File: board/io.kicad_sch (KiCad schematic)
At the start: 14 parts, among them J4 DE9_Socket, J5 DE9_Socket, U15 68681, U16 MAX232, Y2 3.6864MHz

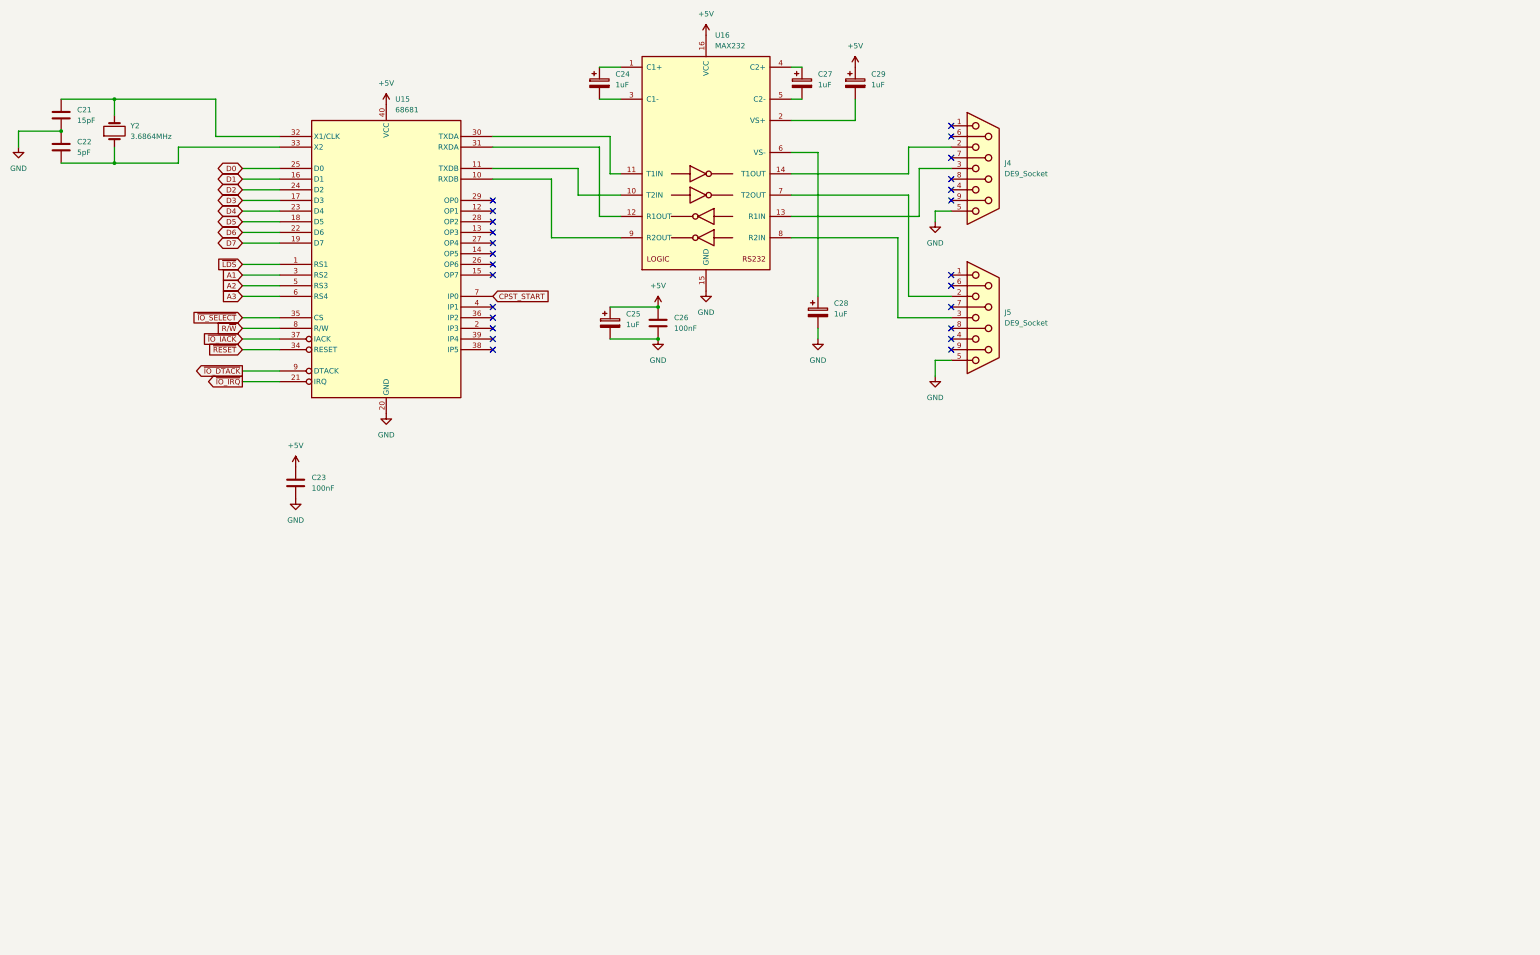
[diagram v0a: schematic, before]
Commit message: change IO to 8051 variant, add audio
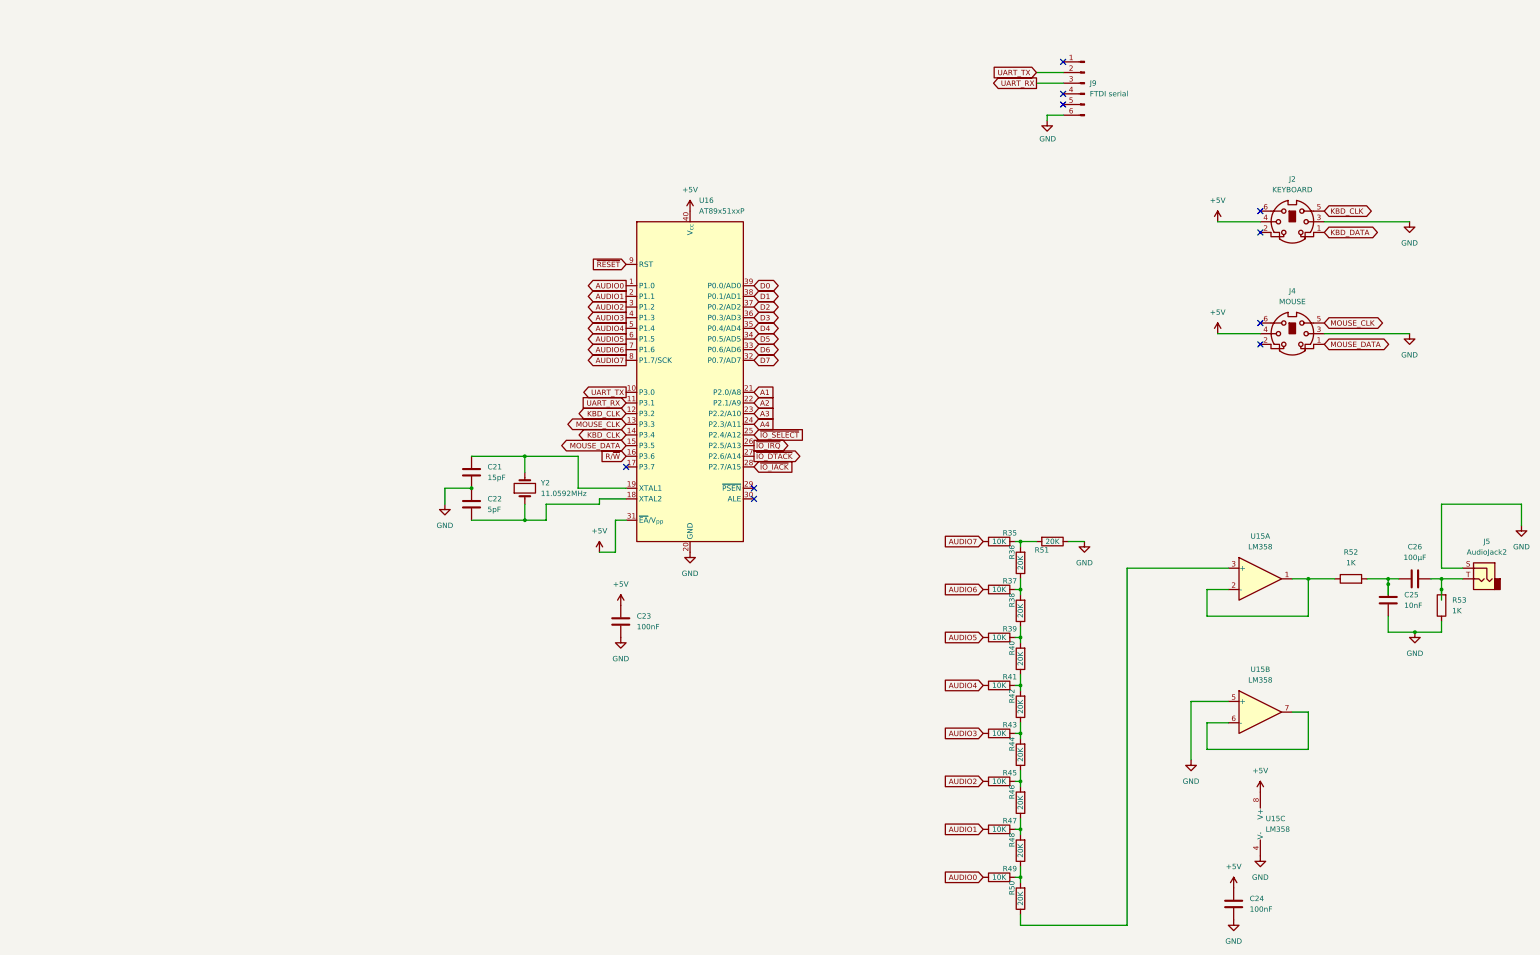
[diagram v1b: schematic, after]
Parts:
- removed C24, C25, C27, C28, C29: 1uF, symbol Device:C_Polarized
- removed J4, J5: DE9_Socket, symbol Connector:DE9_Socket
- removed U15: 68681, symbol Interface:68681
- removed U16: MAX232, symbol Interface_UART:MAX232
- added C24: 100nF, symbol Device:C
- added C25: 10nF, symbol Device:C
- added J2: KEYBOARD, symbol Connector:Mini-DIN-6
- added J4: MOUSE, symbol Connector:Mini-DIN-6
- added J5: AudioJack2, symbol Connector_Audio:AudioJack2
- added J9: FTDI serial, symbol Connector:Conn_01x06_Pin
- added R35, R37, R39, R41, R43, R45, R47, R49: 10K, symbol Device:R
- added R36, R38, R40, R42, R44, R46, R48, R50, R51: 20K, symbol Device:R
- added R52, R53: 1K, symbol Device:R
- added U15: LM358, symbol Amplifier_Operational:LM358
- added U16: AT89x51xxP, Package_DIP:DIP-40_W15.24mm, symbol MCU_Microchip_8051:AT89x51xxP
- C26: value 100nF -> 100µF
- Y2: value 3.6864MHz -> 11.0592MHz
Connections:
- net +5V: now also C24.1, J2.4, J4.4, U15.8 (V+), U16.31 (~{EA}/V_{pp}), U16.40 (V_{cc}); no longer C26.1
- net A1: now also U16.21 (P2.0/A8)
- net A2: now also U16.22 (P2.1/A9)
- net A3: now also U16.23 (P2.2/A10)
- net D0: now also U16.39 (P0.0/AD0)
- net D1: now also U16.38 (P0.1/AD1)
- net D2: now also U16.37 (P0.2/AD2)
- net D3: now also U16.36 (P0.3/AD3)
- net D4: now also U16.35 (P0.4/AD4)
- net D5: now also U16.34 (P0.5/AD5)
- net D6: now also U16.33 (P0.6/AD6)
- net D7: now also U16.32 (P0.7/AD7)
- net GND: now also C24.2, C25.2, J2.3, J4.3, J5.S, J9.6 (Pin_6), R51.1, R53.1, U15.4 (V-), U15.5 (+), U16.20 (GND); no longer C26.2
- net R/~{W}: now also U16.16 (P3.6)
- net ~{IO_DTACK}: now also U16.27 (P2.6/A14)
- net ~{IO_IACK}: now also U16.28 (P2.7/A15)
- net ~{IO_IRQ}: now also U16.26 (P2.5/A13)
- net ~{IO_SELECT}: now also U16.25 (P2.4/A12)
- net ~{RESET}: now also U16.9 (RST)
- net at C21.1, Y2.2: now also U16.19 (XTAL1)
- net at C22.2, Y2.1: now also U16.18 (XTAL2)
- new net: R35.2, R36.2, R51.2
- new net: C25.1, C26.1, R52.2
- new net: C26.2, J5.T, R53.2
- new net: R36.1, R37.2, R38.2
- new net: R44.1, R45.2, R46.2
- new net: R42.1, R43.2, R44.2
- new net: R40.1, R41.2, R42.2
- new net: R38.1, R39.2, R40.2
- new net: U15.6 (-), U15.7
- new net: R46.1, R47.2, R48.2
- new net: R48.1, R49.2, R50.2
- new net: R52.1, U15.1, U15.2 (-)
- new net: R50.1, U15.3 (+)
- new net A4: U16.24 (P2.3/A11)
- new net AUDIO0: R49.1, U16.1 (P1.0)
- new net AUDIO1: R47.1, U16.2 (P1.1)
- new net AUDIO2: R45.1, U16.3 (P1.2)
- new net AUDIO3: R43.1, U16.4 (P1.3)
- new net AUDIO4: R41.1, U16.5 (P1.4)
- new net AUDIO5: R39.1, U16.6 (P1.5)
- new net AUDIO6: R37.1, U16.7 (P1.6)
- new net AUDIO7: R35.1, U16.8 (P1.7/SCK)
- new net KBD_CLK: J2.5, U16.12 (P3.2), U16.14 (P3.4)
- new net KBD_DATA: J2.1
- new net MOUSE_CLK: J4.5, U16.13 (P3.3)
- new net MOUSE_DATA: J4.1, U16.15 (P3.5)
- new net UART_RX: J9.3 (Pin_3), U16.11 (P3.1)
- new net UART_TX: J9.2 (Pin_2), U16.10 (P3.0)
- no-connect marks 25 -> 10
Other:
- moved on the sheet: C21, C22, C23, Y2

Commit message: design draft complete, added footprints
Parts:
- removed J5: AudioJack2, symbol Connector_Audio:AudioJack2
- added J5: AudioJack3, Connector_Audio:Jack_3.5mm_CUI_SJ1-3523N_Horizontal, symbol Connector_Audio:AudioJack3
- added R57, R58: 100, Resistor_THT:R_Axial_DIN0207_L6.3mm_D2.5mm_P10.16mm_Horizontal, symbol Device:R
- C21, C25: footprint (none) -> Capacitor_THT:C_Disc_D3.0mm_W1.6mm_P2.50mm
- C22: value 5pF -> 15pF; footprint (none) -> Capacitor_THT:C_Disc_D3.0mm_W1.6mm_P2.50mm
- C23, C24: footprint (none) -> Capacitor_THT:C_Disc_D5.0mm_W2.5mm_P5.00mm
- C26: footprint (none) -> Capacitor_THT:CP_Radial_D5.0mm_P2.50mm
- J2, J4: footprint (none) -> board:Mini_din6
- J9: footprint (none) -> Connector_PinHeader_2.54mm:PinHeader_1x06_P2.54mm_Vertical
- R35, R36, R37, R38, R39, R40, R41, R42, R43, R44, R45, R46, R47, R48, R49, R50, R51, R52, R53: footprint (none) -> Resistor_THT:R_Axial_DIN0207_L6.3mm_D2.5mm_P10.16mm_Horizontal
- U15: footprint (none) -> Package_DIP:DIP-8_W7.62mm
- Y2: footprint (none) -> Crystal:Resonator-2Pin_W10.0mm_H5.0mm
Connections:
- net GND: now also J5.S
- net KBD_CLK: no longer U16.14 (P3.4)
- net KBD_DATA: now also U16.14 (P3.4)
- net at C26.2, R53.2: now also R57.2, R58.2
- new net: J5.R, R57.1
- new net: J5.T, R58.1

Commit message: start of PCB and MMU
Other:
- moved on the sheet: C21, C22, C23, C24, C25, C26, J2, J4, J5, J9, R35, R36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

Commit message: checkpoint
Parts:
- removed R35, R37, R39, R41, R43, R45, R47, R49: 10K, Resistor_THT:R_Axial_DIN0207_L6.3mm_D2.5mm_P10.16mm_Horizontal, symbol Device:R
- removed R36, R38, R40, R42, R44, R46, R48, R50, R51: 20K, Resistor_THT:R_Axial_DIN0207_L6.3mm_D2.5mm_P10.16mm_Horizontal, symbol Device:R
- added R60: 4610X-R2R-103LF, board:BO_4610X, symbol 68k_board:4610X-R2R-103LF
- J2, J4: symbol Connector:Mini-DIN-6 -> 68k_board:Mini-DIN-6-GroundPins
- J9: footprint Connector_PinHeader_2.54mm:PinHeader_1x06_P2.54mm_Vertical -> Connector_PinHeader_2.54mm:PinHeader_1x06_P2.54mm_Horizontal
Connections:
- net AUDIO0: now also R60.9
- net AUDIO1: now also R60.8
- net AUDIO2: now also R60.7
- net AUDIO3: now also R60.6
- net AUDIO4: now also R60.5
- net AUDIO5: now also R60.4
- net AUDIO6: now also R60.3
- net AUDIO7: now also R60.2
- net GND: now also J2.7 (GND), J4.7 (GND), R60.10
- net at U15.3 (+): now also R60.1

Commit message: checkpoint
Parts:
- removed C24: 100nF, Capacitor_THT:C_Disc_D5.0mm_W2.5mm_P5.00mm, symbol Device:C
- removed C25: 10nF, Capacitor_THT:C_Disc_D3.0mm_W1.6mm_P2.50mm, symbol Device:C
- removed C26: 100µF, Capacitor_THT:CP_Radial_D5.0mm_P2.50mm, symbol Device:C
- removed J5: AudioJack3, Connector_Audio:Jack_3.5mm_CUI_SJ1-3523N_Horizontal, symbol Connector_Audio:AudioJack3
- removed R52, R53: 1K, Resistor_THT:R_Axial_DIN0207_L6.3mm_D2.5mm_P10.16mm_Horizontal, symbol Device:R
- removed R57, R58: 100, Resistor_THT:R_Axial_DIN0207_L6.3mm_D2.5mm_P10.16mm_Horizontal, symbol Device:R
- removed R60: 4610X-R2R-103LF, board:BO_4610X, symbol 68k_board:4610X-R2R-103LF
- removed U15: LM358, Package_DIP:DIP-8_W7.62mm, symbol Amplifier_Operational:LM358
- added R7, R9: 10K, Resistor_THT:R_Axial_DIN0207_L6.3mm_D2.5mm_P10.16mm_Horizontal, symbol Device:R
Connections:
- net ~{IO_SELECT} is gone; now on net ~{IO_IRQ}: U16.25 (P2.4/A12)
- net +5V: now also R7.1, R9.1
- net KBD_CLK: now also U16.13 (P3.3); no longer U16.12 (P3.2)
- net KBD_DATA: now also U16.12 (P3.2); no longer U16.14 (P3.4)
- net MOUSE_CLK: now also U16.15 (P3.5); no longer U16.13 (P3.3)
- net MOUSE_DATA: now also U16.14 (P3.4); no longer U16.15 (P3.5)
- net ~{IO_IRQ}: now also R7.2; no longer U16.26 (P2.5/A13)
- net AUDIO0: no longer names the net of U16.1 (P1.0)
- net AUDIO1: no longer names the net of U16.2 (P1.1)
- net AUDIO2: no longer names the net of U16.3 (P1.2)
- net AUDIO3: no longer names the net of U16.4 (P1.3)
- net AUDIO4: no longer names the net of U16.5 (P1.4)
- net AUDIO5 renamed ~{IO_SELECT_MOSI}
- net AUDIO6 renamed ~{IO_DTACK_MISO}
- net AUDIO7 renamed ~{IO_IACK_SCK}
- net ~{IO_DTACK}: no longer names the net of U16.27 (P2.6/A14)
- net ~{IO_IACK}: no longer names the net of U16.28 (P2.7/A15)
- net ~{RESET} renamed IO_RESET
- net IO_RESET: now also R9.2
- no-connect marks 10 -> 18

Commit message: Board rev1 PCB complete, already have a spot fix
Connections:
- net A1: now also U16.39 (P0.0/AD0); no longer U16.21 (P2.0/A8)
- net A2: now also U16.38 (P0.1/AD1); no longer U16.22 (P2.1/A9)
- net A3: now also U16.37 (P0.2/AD2); no longer U16.23 (P2.2/A10)
- net A4: now also U16.36 (P0.3/AD3); no longer U16.24 (P2.3/A11)
- net D0: now also U16.21 (P2.0/A8); no longer U16.39 (P0.0/AD0)
- net D1: now also U16.22 (P2.1/A9); no longer U16.38 (P0.1/AD1)
- net D2: now also U16.23 (P2.2/A10); no longer U16.37 (P0.2/AD2)
- net D3: now also U16.24 (P2.3/A11); no longer U16.36 (P0.3/AD3)
- net D4: now also U16.25 (P2.4/A12); no longer U16.35 (P0.4/AD4)
- net D5: now also U16.26 (P2.5/A13); no longer U16.34 (P0.5/AD5)
- net D6: now also U16.27 (P2.6/A14); no longer U16.33 (P0.6/AD6)
- net D7: now also U16.28 (P2.7/A15); no longer U16.32 (P0.7/AD7)
- net ~{IO_IRQ}: now also U16.34 (P0.5/AD5); no longer U16.25 (P2.4/A12)
- new net A5: U16.35 (P0.4/AD4)
- no-connect marks 18 -> 17
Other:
- moved on the sheet: R7
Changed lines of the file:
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@@
 	(paper "USLetter")
 	(junction
-		(at 104.14 113.03)
+		(at 104.14 90.17)
 		(diameter 0)
 		(color 0 0 0 0)
@@
 	)
 	(no_connect
-		(at 90.17 120.65)
+		(at 90.17 95.25)
 	)
 	(no_connect
@@
 	)
 	(no_connect
-		(at 90.17 115.57)
-	)
-	(no_connect
 		(at 59.69 80.01)
 	)
@@
 	)
 	(no_connect
-		(at 90.17 118.11)
+		(at 90.17 92.71)
 	)
 	(no_connect
@@
 	(wire
 		(pts
-			(xy 114.3 113.03) (xy 104.14 113.03)
+			(xy 114.3 90.17) (xy 104.14 90.17)
 		)
 		(stroke
@@
 	(wire
 		(pts
-			(xy 104.14 113.03) (xy 90.17 113.03)
+			(xy 104.14 90.17) (xy 90.17 90.17)
 		)
 		(stroke
@@
 	(wire
 		(pts
-			(xy 104.14 106.68) (xy 104.14 113.03)
+			(xy 104.14 83.82) (xy 104.14 90.17)
 		)
 		(stroke
@@
 	(global_label "A1"
 		(shape input)
-		(at 90.17 102.87 0)
+		(at 90.17 77.47 0)
 		(fields_autoplaced yes)
 		(effects
@@
 		)
 		(property "Intersheetrefs" "${INTERSHEET_REFS}"
-			(at 95.4533 102.87 0)
+			(at 95.4533 77.47 0)
 			(effects
 				(font
@@
 	(global_label "D0"
 		(shape tri_state)
-		(at 90.17 77.47 0)
+		(at 90.17 102.87 0)
 		(fields_autoplaced yes)
 		(effects
@@
 		)
 		(property "Intersheetrefs" "${INTERSHEET_REFS}"
-			(at 96.746 77.47 0)
+			(at 96.746 102.87 0)
 			(effects
 				(font
@@
 	(global_label "D2"
 		(shape tri_state)
-		(at 90.17 82.55 0)
+		(at 90.17 107.95 0)
 		(fields_autoplaced yes)
 		(effects
@@
 		)
 		(property "Intersheetrefs" "${INTERSHEET_REFS}"
-			(at 96.746 82.55 0)
+			(at 96.746 107.95 0)
 			(effects
 				(font
@@
 	(global_label "~{IO_IRQ}"
 		(shape output)
-		(at 114.3 113.03 0)
+		(at 114.3 90.17 0)
 		(fields_autoplaced yes)
 		(effects
@@
 		)
 		(property "Intersheetrefs" "${INTERSHEET_REFS}"
-			(at 123.3934 113.03 0)
+			(at 123.3934 90.17 0)
 			(effects
 				(font
@@
 	(global_label "D5"
 		(shape tri_state)
-		(at 90.17 90.17 0)
+		(at 90.17 115.57 0)
 		(fields_autoplaced yes)
 		(effects
@@
 		)
 		(property "Intersheetrefs" "${INTERSHEET_REFS}"
-			(at 96.746 90.17 0)
+			(at 96.746 115.57 0)
+			(effects
+				(font
+					(size 1.27 1.27)
+				)
+				(justify left)
+				(hide yes)
+			)
+		)
+	)
+	(global_label "A5"
+		(shape input)
+		(at 90.17 87.63 0)
+		(fields_autoplaced yes)
+		(effects
+			(font
+				(size 1.27 1.27)
+			)
+			(justify left)
+		)
+		(property "Intersheetrefs" "${INTERSHEET_REFS}"
+			(at 95.4533 87.63 0)
 			(effects
 				(font
@@
 	(global_label "D6"
 		(shape tri_state)
-		(at 90.17 92.71 0)
+		(at 90.17 118.11 0)
 		(fields_autoplaced yes)
 		(effects
@@
 		)
 		(property "Intersheetrefs" "${INTERSHEET_REFS}"
-			(at 96.746 92.71 0)
+			(at 96.746 118.11 0)
 			(effects
 				(font
@@
 	(global_label "D1"
 		(shape tri_state)
-		(at 90.17 80.01 0)
+		(at 90.17 105.41 0)
 		(fields_autoplaced yes)
 		(effects
@@
 		)
 		(property "Intersheetrefs" "${INTERSHEET_REFS}"
-			(at 96.746 80.01 0)
+			(at 96.746 105.41 0)
 			(effects
 				(font
@@
 	(global_label "A3"
 		(shape input)
-		(at 90.17 107.95 0)
+		(at 90.17 82.55 0)
 		(fields_autoplaced yes)
 		(effects
@@
 		)
 		(property "Intersheetrefs" "${INTERSHEET_REFS}"
-			(at 95.4533 107.95 0)
+			(at 95.4533 82.55 0)
 			(effects
 				(font
@@
 	(global_label "D3"
 		(shape tri_state)
-		(at 90.17 85.09 0)
+		(at 90.17 110.49 0)
 		(fields_autoplaced yes)
 		(effects
@@
 		)
 		(property "Intersheetrefs" "${INTERSHEET_REFS}"
-			(at 96.746 85.09 0)
+			(at 96.746 110.49 0)
 			(effects
 				(font
@@
 	(global_label "D4"
 		(shape tri_state)
-		(at 90.17 87.63 0)
+		(at 90.17 113.03 0)
 		(fields_autoplaced yes)
 		(effects
@@
 		)
 		(property "Intersheetrefs" "${INTERSHEET_REFS}"
-			(at 96.746 87.63 0)
+			(at 96.746 113.03 0)
 			(effects
 				(font
@@
 	(global_label "A4"
 		(shape input)
-		(at 90.17 110.49 0)
+		(at 90.17 85.09 0)
 		(fields_autoplaced yes)
 		(effects
@@
 		)
 		(property "Intersheetrefs" "${INTERSHEET_REFS}"
-			(at 95.4533 110.49 0)
+			(at 95.4533 85.09 0)
 			(effects
 				(font
@@
 	(global_label "D7"
 		(shape tri_state)
-		(at 90.17 95.25 0)
+		(at 90.17 120.65 0)
 		(fields_autoplaced yes)
 		(effects
@@
 		)
 		(property "Intersheetrefs" "${INTERSHEET_REFS}"
-			(at 96.746 95.25 0)
+			(at 96.746 120.65 0)
 			(effects
 				(font
@@
 	(global_label "A2"
 		(shape input)
-		(at 90.17 105.41 0)
+		(at 90.17 80.01 0)
 		(fields_autoplaced yes)
 		(effects
@@
 		)
 		(property "Intersheetrefs" "${INTERSHEET_REFS}"
-			(at 95.4533 105.41 0)
+			(at 95.4533 80.01 0)
 			(effects
 				(font
@@
 	(symbol
 		(lib_id "Device:R")
-		(at 104.14 102.87 0)
+		(at 104.14 80.01 0)
 		(unit 1)
 		(exclude_from_sim no)
@@
 		(dnp no)
 		(property "Reference" "R7"
-			(at 98.298 101.346 0)
+			(at 98.298 78.486 0)
 			(effects
 				(font
@@
 		)
 		(property "Value" "10K"
-			(at 98.552 104.14 0)
+			(at 98.552 81.28 0)
 			(effects
 				(font
@@
 		)
 		(property "Footprint" "Resistor_THT:R_Axial_DIN0207_L6.3mm_D2.5mm_P10.16mm_Horizontal"
-			(at 102.362 102.87 90)
+			(at 102.362 80.01 90)
 			(effects
 				(font
@@
 		)
 		(property "Datasheet" "~"
-			(at 104.14 102.87 0)
+			(at 104.14 80.01 0)
 			(effects
 				(font
@@
 		)
 		(property "Description" "Resistor"
-			(at 104.14 102.87 0)
+			(at 104.14 80.01 0)
 			(effects
 				(font
@@
 	(symbol
 		(lib_id "power:+5V")
-		(at 104.14 99.06 0)
+		(at 104.14 76.2 0)
 		(unit 1)
 		(exclude_from_sim no)
@@
 		(fields_autoplaced yes)
 		(property "Reference" "#PWR082"
-			(at 104.14 102.87 0)
+			(at 104.14 80.01 0)
 			(effects
 				(font
@@
 		)
 		(property "Value" "+5V"
-			(at 104.14 93.98 0)
+			(at 104.14 71.12 0)
 			(effects
 				(font
@@
 		)
 		(property "Footprint" ""
-			(at 104.14 99.06 0)
+			(at 104.14 76.2 0)
 			(effects
 				(font
@@
 		)
 		(property "Datasheet" ""
-			(at 104.14 99.06 0)
+			(at 104.14 76.2 0)
 			(effects
 				(font
@@
 		)
 		(property "Description" "Power symbol creates a global label with name \"+5V\""
-			(at 104.14 99.06 0)
-			(effects
-				(font
+			(at 104.14 76.2 0)
+			(effects
+				(font
